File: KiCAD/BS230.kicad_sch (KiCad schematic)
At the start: 20 parts

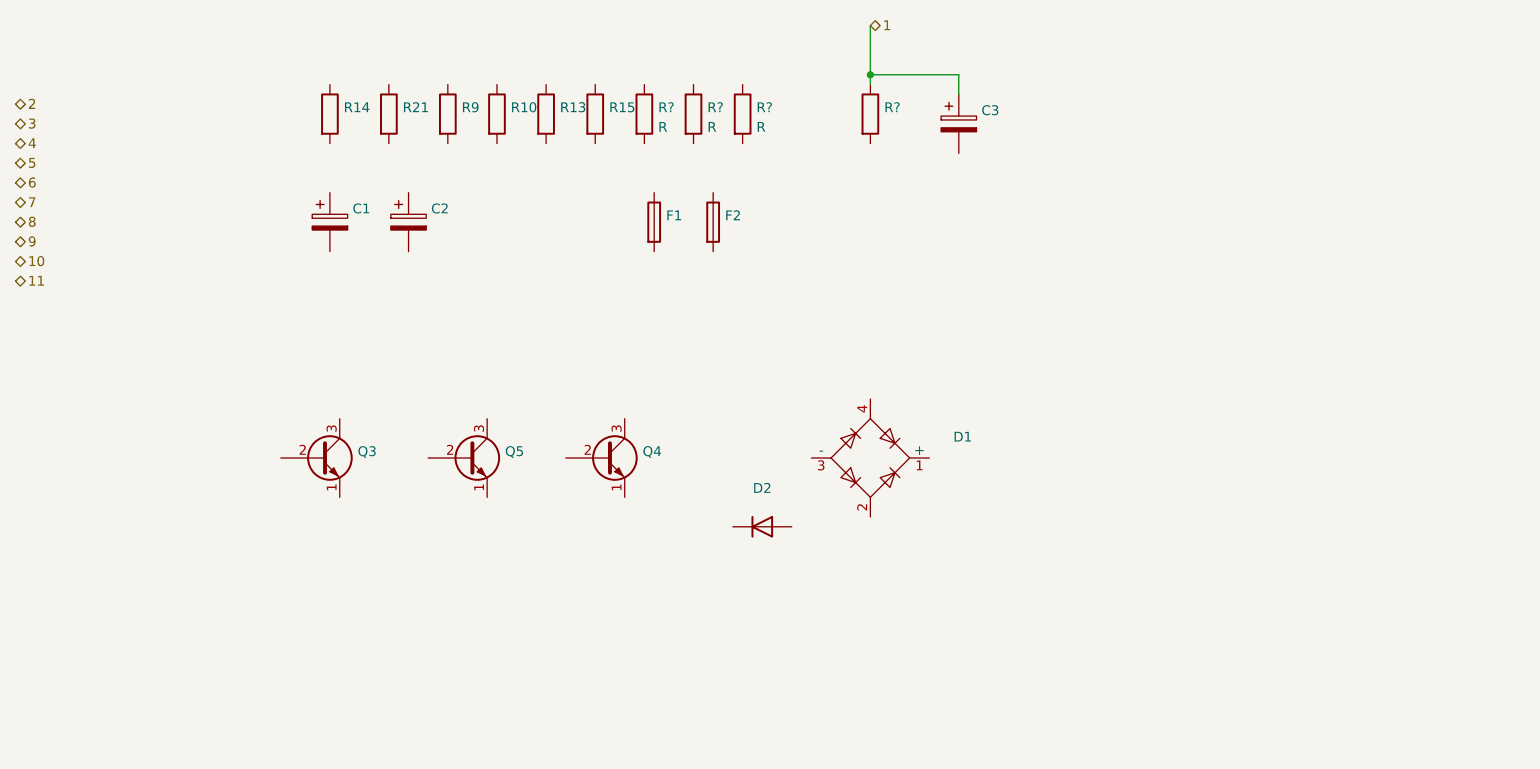
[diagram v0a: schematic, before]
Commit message: Schematics for BS112, BS230 and BS263 added
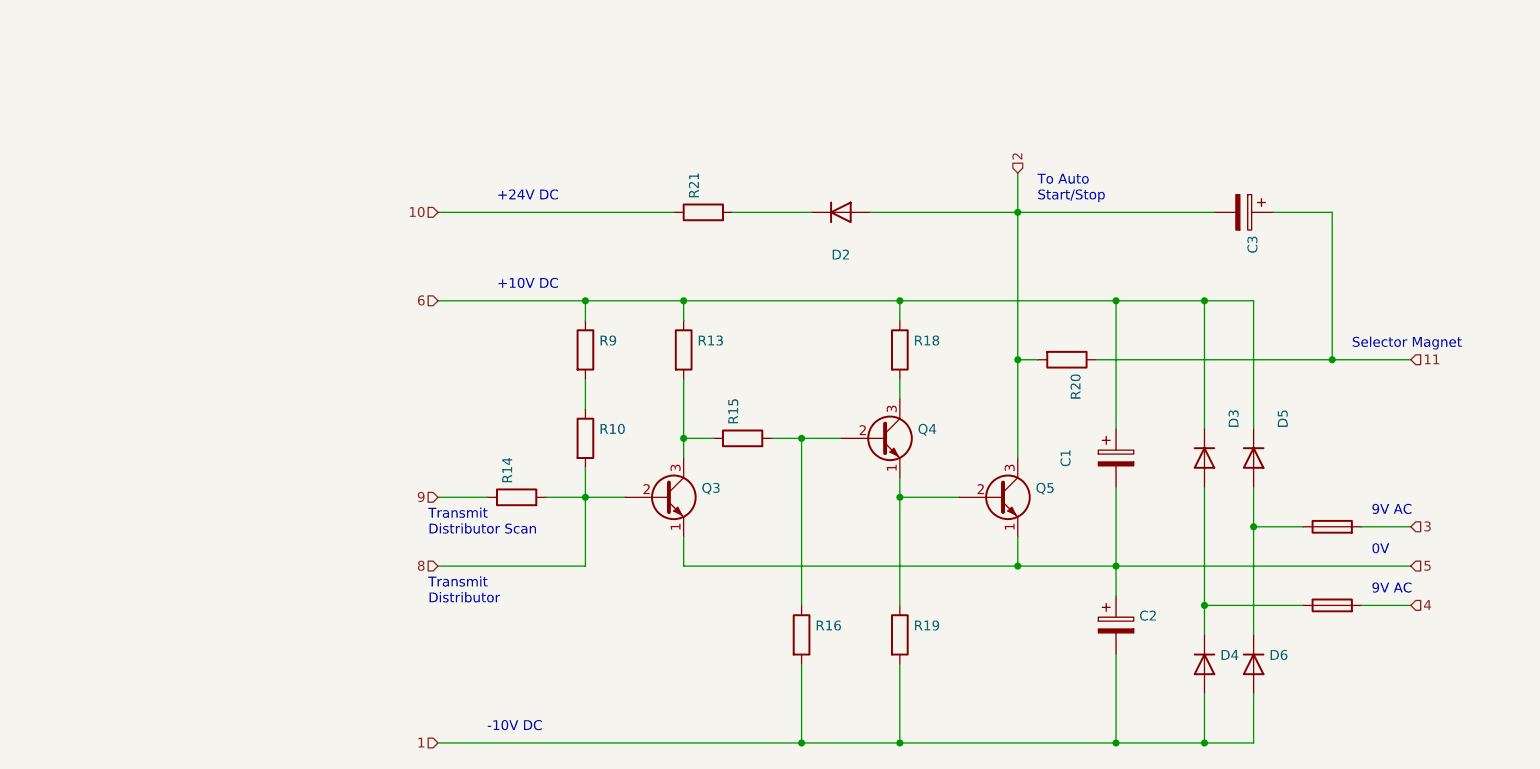
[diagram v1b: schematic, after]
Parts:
- removed D1: (no value), symbol Diode_Bridge:B250C1500G
- removed D2: (no value), symbol Diode:1N4007
- removed R? (x3): R, symbol Device:R
- removed R?: (no value), symbol Device:R
- added D2, D3, D4, D5, D6: (no value), symbol Device:D
- added R16, R18, R19, R20: (no value), symbol Device:R
- C1, C2: value (none) -> ~
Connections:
- net 1: now also C2.2, D4.2 (A), D6.2 (A), R16.2, R19.2; no longer C3.1
- net 10: now also R21.1
- net 11: now also C3.1, R20.1
- net 2: now also C3.2, Q5.3 (C), D2.2 (A), R20.2
- net 3: now also F1.2
- net 4: now also F2.2
- net 5: now also C1.2, C2.1, Q3.1 (E), Q5.1 (E)
- net 6: now also C1.1, R13.1, R9.1, D3.1 (K), D5.1 (K), R18.1
- net 8: now also Q3.2 (B), R10.2, R14.2
- net 9: now also R14.1
- net at R15.1: now also Q3.3 (C), R13.2
- net at R15.2: now also Q4.2 (B), R16.1
- net at F2.1: now also D3.2 (A), D4.1 (K)
- net at Q4.1 (E): now also Q5.2 (B), R19.1
- net at Q4.3 (C): now also R18.2
- net at R9.2: now also R10.1
- net at R21.2: now also D2.1 (K)
- net at F1.1: now also D5.2 (A), D6.1 (K)
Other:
- note added: "+10V DC"
- note added: "+24V DC"
- note added: "-10V DC"
- note added: "0V"
- note added: "9V AC"
- note added: "Selector Magnet"
- note added: "To Auto Start/Stop"
- note added: "Transmit Distributor"
- note added: "Transmit Distributor Scan"

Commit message: Connections finished
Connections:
- net 1 renamed 1 -10V
- net 10 renamed 10 +24V
- net 11 renamed 11 Sel Mag
- net 2 renamed 2 Auto Start
- net 3 renamed 3 9VAC
- net 4 renamed 4 9VAC
- net 5 renamed 5 0V
- net 6 renamed 6 +10V
- net 8 renamed 8 Tx Distr
- net 9 renamed 9 TX Distr Scan
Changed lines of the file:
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@@
     (effects (font (size 1.27 1.27)) (justify left bottom))
   )
-  (hierarchical_label "2" (shape input) (at 195.58 59.69 90)
+  (hierarchical_label "2 Auto Start" (shape output) (at 195.58 59.69 90)
     (effects (font (size 1.27 1.27)) (justify left))
   )
-  (hierarchical_label "1" (shape input) (at 120.65 133.35 180)
+  (hierarchical_label "1 -10V" (shape output) (at 120.65 133.35 180)
     (effects (font (size 1.27 1.27)) (justify right))
   )
-  (hierarchical_label "4" (shape input) (at 246.38 115.57 0)
+  (hierarchical_label "4 9VAC" (shape input) (at 246.38 115.57 0)
     (effects (font (size 1.27 1.27)) (justify left))
   )
-  (hierarchical_label "5" (shape input) (at 246.38 110.49 0)
+  (hierarchical_label "5 0V" (shape input) (at 246.38 110.49 0)
     (effects (font (size 1.27 1.27)) (justify left))
   )
-  (hierarchical_label "3" (shape input) (at 246.38 105.41 0)
+  (hierarchical_label "3 9VAC" (shape input) (at 246.38 105.41 0)
     (effects (font (size 1.27 1.27)) (justify left))
   )
-  (hierarchical_label "10" (shape input) (at 120.65 64.77 180)
+  (hierarchical_label "10 +24V" (shape input) (at 120.65 64.77 180)
     (effects (font (size 1.27 1.27)) (justify right))
   )
-  (hierarchical_label "8" (shape input) (at 120.65 110.49 180)
+  (hierarchical_label "8 Tx Distr" (shape input) (at 120.65 110.49 180)
     (effects (font (size 1.27 1.27)) (justify right))
   )
-  (hierarchical_label "11" (shape input) (at 246.38 83.82 0)
+  (hierarchical_label "11 Sel Mag" (shape output) (at 246.38 83.82 0)
     (effects (font (size 1.27 1.27)) (justify left))
   )
-  (hierarchical_label "9" (shape input) (at 120.65 101.6 180)
+  (hierarchical_label "9 TX Distr Scan" (shape input) (at 120.65 101.6 180)
     (effects (font (size 1.27 1.27)) (justify right))
   )
-  (hierarchical_label "6" (shape input) (at 120.65 76.2 180)
+  (hierarchical_label "6 +10V" (shape output) (at 120.65 76.2 180)
     (effects (font (size 1.27 1.27)) (justify right))
   )
@@
   (symbol (lib_id "Device:D") (at 219.71 123.19 270) (unit 1)
     (in_bom yes) (on_board yes)
-    (property "Reference" "D4" (id 0) (at 221.742 122.0216 90)
+    (property "Reference" "D4" (id 0) (at 214.63 121.92 90)
       (effects (font (size 1.27 1.27)) (justify left))
     )
-    (property "Value" "" (id 1) (at 221.742 124.333 90)
+    (property "Value" "" (id 1) (at 212.09 124.46 90)
       (effects (font (size 1.27 1.27)) (justify left))
     )

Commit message: Labels
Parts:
- C3: value (none) -> 40u
- D2, D3, D4, D5, D6: value (none) -> ZS70
- F1, F2: value (none) -> 1.5A
- Q3, Q5: value (none) -> BFY51
- Q4: value (none) -> BSV95A
- R10: value (none) -> 750
- R13: value (none) -> 1R5
- R14, R18: value (none) -> 220
- R15: value (none) -> 2k2
- R16: value (none) -> 22k
- R19: value (none) -> 47k
- R20, R21: value (none) -> 47
- R9: value (none) -> 150
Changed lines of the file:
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@@
     (in_bom yes) (on_board yes)
     (property "Reference" "D5" (id 0) (at 229.87 91.44 0))
-    (property "Value" "" (id 1) (at 227.33 90.17 0))
+    (property "Value" "ZS70" (id 1) (at 227.33 90.17 0))
     (property "Footprint" "" (id 2) (at 226.06 96.52 0)
       (effects (font (size 1.27 1.27)) hide)
@@
     (in_bom yes) (on_board yes)
     (property "Reference" "D3" (id 0) (at 223.52 91.44 0))
-    (property "Value" "" (id 1) (at 220.98 90.17 0))
+    (property "Value" "ZS70" (id 1) (at 220.98 90.17 0))
     (property "Footprint" "" (id 2) (at 219.71 96.52 0)
       (effects (font (size 1.27 1.27)) hide)
@@
       (effects (font (size 1.27 1.27)) (justify left))
     )
-    (property "Value" "" (id 1) (at 228.092 124.333 90)
+    (property "Value" "ZS70" (id 1) (at 228.092 124.333 90)
       (effects (font (size 1.27 1.27)) (justify left))
     )
@@
       (effects (font (size 1.27 1.27)) (justify left))
     )
-    (property "Value" "" (id 1) (at 212.09 124.46 90)
+    (property "Value" "ZS70" (id 1) (at 212.09 124.46 90)
       (effects (font (size 1.27 1.27)) (justify left))
     )
@@
     (in_bom yes) (on_board yes)
     (property "Reference" "D2" (id 0) (at 172.72 70.2818 0))
-    (property "Value" "" (id 1) (at 172.72 67.9704 0))
+    (property "Value" "ZS70" (id 1) (at 172.72 67.9704 0))
     (property "Footprint" "" (id 2) (at 172.72 64.77 0)
       (effects (font (size 1.27 1.27)) hide)
@@
       (effects (font (size 1.27 1.27)) (justify left) hide)
     )
-    (property "Value" "" (id 1) (at 236.22 112.903 90))
+    (property "Value" "1.5A" (id 1) (at 236.22 112.903 90))
     (property "Footprint" "" (id 2) (at 236.22 117.348 90)
       (effects (font (size 1.27 1.27)) hide)
@@
       (effects (font (size 1.27 1.27)) hide)
     )
-    (property "Value" "" (id 1) (at 236.22 102.743 90))
+    (property "Value" "1.5A" (id 1) (at 236.22 102.743 90))
     (property "Footprint" "" (id 2) (at 236.22 107.188 90)
       (effects (font (size 1.27 1.27)) hide)
@@
       (effects (font (size 1.27 1.27)) (justify left))
     )
-    (property "Value" "" (id 1) (at 182.6514 95.123 0)
+    (property "Value" "BSV95A" (id 1) (at 182.6514 95.123 0)
       (effects (font (size 1.27 1.27)) (justify left))
     )
@@
       (effects (font (size 1.27 1.27)) (justify left))
     )
-    (property "Value" "" (id 1) (at 197.8914 102.743 0)
+    (property "Value" "BFY51" (id 1) (at 197.8914 102.743 0)
       (effects (font (size 1.27 1.27)) (justify left))
     )
@@
       (effects (font (size 1.27 1.27)) (justify left))
     )
-    (property "Value" "" (id 1) (at 154.7114 102.743 0)
+    (property "Value" "BFY51" (id 1) (at 154.7114 102.743 0)
       (effects (font (size 1.27 1.27)) (justify left))
     )
@@
       (effects (font (size 1.27 1.27)) (justify left))
     )
-    (property "Value" "" (id 1) (at 156.083 62.992 0)
+    (property "Value" "47" (id 1) (at 156.083 62.992 0)
       (effects (font (size 1.27 1.27)) (justify left))
     )
@@
       (effects (font (size 1.27 1.27)) (justify left))
     )
-    (property "Value" "" (id 1) (at 141.478 83.693 0)
+    (property "Value" "150" (id 1) (at 141.478 83.693 0)
       (effects (font (size 1.27 1.27)) (justify left))
     )
@@
       (effects (font (size 1.27 1.27)) (justify left))
     )
-    (property "Value" "" (id 1) (at 154.178 83.693 0)
+    (property "Value" "1R5" (id 1) (at 154.178 83.693 0)
       (effects (font (size 1.27 1.27)) (justify left))
     )
@@
       (effects (font (size 1.27 1.27)) (justify left))
     )
-    (property "Value" "" (id 1) (at 161.163 92.202 0)
+    (property "Value" "2k2" (id 1) (at 161.163 92.202 0)
       (effects (font (size 1.27 1.27)) (justify left))
     )
@@
       (effects (font (size 1.27 1.27)) (justify left))
     )
-    (property "Value" "" (id 1) (at 200.787 85.598 0)
+    (property "Value" "47" (id 1) (at 200.787 85.598 0)
       (effects (font (size 1.27 1.27)) (justify left))
     )
@@
       (effects (font (size 1.27 1.27)) (justify left))
     )
-    (property "Value" "" (id 1) (at 182.118 83.693 0)
+    (property "Value" "220" (id 1) (at 182.118 83.693 0)
       (effects (font (size 1.27 1.27)) (justify left))
     )
@@
       (effects (font (size 1.27 1.27)) (justify left))
     )
-    (property "Value" "" (id 1) (at 169.418 120.523 0)
+    (property "Value" "22k" (id 1) (at 169.418 120.523 0)
       (effects (font (size 1.27 1.27)) (justify left))
     )
@@
       (effects (font (size 1.27 1.27)) (justify left))
     )
-    (property "Value" "" (id 1) (at 131.953 99.822 0)
+    (property "Value" "220" (id 1) (at 131.953 99.822 0)
       (effects (font (size 1.27 1.27)) (justify left))
     )
@@
       (effects (font (size 1.27 1.27)) (justify left))
     )
-    (property "Value" "" (id 1) (at 141.478 95.123 0)
+    (property "Value" "750" (id 1) (at 141.478 95.123 0)
       (effects (font (size 1.27 1.27)) (justify left))
     )
@@
       (effects (font (size 1.27 1.27)) (justify left))
     )
-    (property "Value" "" (id 1) (at 182.118 120.523 0)
+    (property "Value" "47k" (id 1) (at 182.118 120.523 0)
       (effects (font (size 1.27 1.27)) (justify left))
     )
@@
       (effects (font (size 1.27 1.27)) (justify left))
     )
-    (property "Value" "" (id 1) (at 223.647 67.7672 0)
-      (effects (font (size 1.27 1.27)) (justify left))
-    )
+    (property "Value" "40u" (id 1) (at 223.647 67.7672 0)
+      (effects (font (size 1.27 1.27)) (justify left))
+    )

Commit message: Labels added
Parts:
- C1, C2: value ~ -> (none)
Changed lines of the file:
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@@
   (symbol (lib_id "Device:C_Polarized") (at 208.28 96.52 0) (unit 1)
     (in_bom yes) (on_board yes)
-    (property "Reference" "C1" (id 0) (at 201.803 96.52 90))
-    (property "Value" "~" (id 1) (at 204.1144 96.52 90))
+    (property "Reference" "C1" (id 0) (at 212.09 91.44 0))
+    (property "Value" "" (id 1) (at 213.36 93.98 0))
     (property "Footprint" "" (id 2) (at 209.2452 100.33 0)
       (effects (font (size 1.27 1.27)) hide)
@@
       (effects (font (size 1.27 1.27)) (justify left))
     )
-    (property "Value" "~" (id 1) (at 211.2772 119.253 0)
+    (property "Value" "" (id 1) (at 211.2772 119.253 0)
       (effects (font (size 1.27 1.27)) (justify left))
     )
